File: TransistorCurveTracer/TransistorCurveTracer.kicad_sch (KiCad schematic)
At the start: 24 parts, among them J1 Conn_01x04_Pin, J2 Conn_01x04_Pin, J3 Conn_01x04_Pin, Q1 BC547, U1 NE555P, U3 MCP601-xP

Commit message: in progress
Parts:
- added Q2: BC547, Package_TO_SOT_THT:TO-92_Inline, symbol Transistor_BJT:BC547
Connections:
- net GND: now also Q2.3 (E)
- net Pulse1: now also Q2.2 (B)
- net NC renamed ResetStairStep
- net ResetStairStep: now also Q2.1 (C)
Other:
- note added: "Module 1 NE555"
- note added: "Module2 Reset NE555 + reset StairStep"
- moved on the sheet: C1, C2, C3, C4, D1, D2, D3, D4, J1, J2, J3, Q1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

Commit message: in progress
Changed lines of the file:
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@@
       (effects (font (size 1.27 1.27)) (justify left))
     )
-    (property "Value" "6.8k" (at 149.86 92.71 0)
+    (property "Value" "6.8k" (at 149.86 93.98 0)
       (effects (font (size 1.27 1.27)) (justify left))
     )

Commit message: curve tracer in progress
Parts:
- added C5: 100n, Capacitor_SMD:C_0805_2012Metric_Pad1.18x1.45mm_HandSolder, symbol Device:C
- added C6: 10n, Capacitor_SMD:C_1206_3216Metric_Pad1.33x1.80mm_HandSolder, symbol Device:C
- added Q3: BC547, Package_TO_SOT_THT:TO-92_Inline, symbol Transistor_BJT:BC547
- added Q4, Q5: 2N2907, symbol Simulation_SPICE:PNP
- added Q6: DUT, Package_TO_SOT_THT:TO-92_Inline, symbol Transistor_BJT:BC547
- added R11, R12, R13, R14, R15, R18: 10k, Resistor_SMD:R_1206_3216Metric_Pad1.30x1.75mm_HandSolder, symbol Device:R
- added R16, R17: 3.9k, Resistor_SMD:R_1206_3216Metric_Pad1.30x1.75mm_HandSolder, symbol Device:R
- added R19: 470k, Resistor_SMD:R_1206_3216Metric_Pad1.30x1.75mm_HandSolder, symbol Device:R
- added R20: 270k, Resistor_SMD:R_1206_3216Metric_Pad1.30x1.75mm_HandSolder, symbol Device:R
- added U2, U4: MCP601-xP, Package_DIP:DIP-8_W7.62mm, symbol Amplifier_Operational:MCP601-xP
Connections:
- net GND: now also U3.7 (V+), C5.2, C6.2, Q3.3 (E), Q6.3 (E), R12.2, R17.2, R20.2, U2.7 (V+), U4.7 (V+); no longer U3.4 (V-)
- net Out555: now also R11.2, R16.2
- net ResetStairStep: now also C5.1, R11.1, R14.2, U2.3 (+)
- net Vcc: now also U3.4 (V-), R15.1, U2.4 (V-), U4.4 (V-); no longer U3.7 (V+)
- net at R1.1, R2.1, R3.1: now also U3.3 (+); no longer U3.2 (-)
- net at C1.1, D1.1 (K), D2.2 (A): now also U3.2 (-); no longer U3.3 (+)
- new net: R12.1, R13.2, U2.2 (-)
- new net: R17.1, R18.2, U4.2 (-)
- new net: C6.1, Q3.1 (C), R15.2, U4.3 (+)
- new net: Q6.2 (B), R19.2
- new net: Q3.2 (B), R16.1
- new net SawTooth: Q4.3 (E), Q5.3 (E), R18.1, U4.6
- new net StairStep: R13.1, R14.1, R19.1, U2.6
- new net X: Q4.1 (C), Q4.2 (B), Q5.2 (B), Q6.1 (C)
- new net Y: Q5.1 (C), R20.1
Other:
- note added: "In1 : StairStep In2 : GNG In3 : SawTooth Out1 : X Out2 : Y"
- note added: "In1 : Vcc In2 : GND In3 : Out555 In4 : ResetStairStep Out : StairStep"
- note added: "In1 : Vcc In2 : GND In3 : Out555 Out : SawTooth"
- note added: "In1 : Vcc In2 : GND In3 : Reset555 Out : Out555"
- note added: "In1 : Vcc In2 : GND Out1: ResetStairStep Out2: Reset555"
- note added: "Module 3 StairStep"
- note added: "Module 4 SawTooth"
- note added: "Module 5 Out X Y"

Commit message: TransistorCurveTracer in progress
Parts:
- added J4: Conn_01x04_Pin, Connector_PinHeader_2.54mm:PinHeader_1x04_P2.54mm_Vertical, symbol Connector:Conn_01x04_Pin
- added J5, J6: Conn_01x05_Pin, Connector_PinHeader_2.54mm:PinHeader_1x05_P2.54mm_Vertical, symbol Connector:Conn_01x05_Pin
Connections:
- net GND: now also J4.2 (Pin_2), J5.2 (Pin_2), J6.2 (Pin_2)
- net Out555: now also J4.3 (Pin_3), J5.3 (Pin_3)
- net ResetStairStep: now also J5.4 (Pin_4)
- net SawTooth: now also J4.4 (Pin_4), J6.3 (Pin_3)
- net StairStep: now also J5.5 (Pin_5), J6.1 (Pin_1)
- net Vcc: now also J4.1 (Pin_1), J5.1 (Pin_1)
- net X: now also J6.4 (Pin_4)
- net Y: now also J6.5 (Pin_5)
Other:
- moved on the sheet: C5, C6, Q3, Q4, Q5, Q6, R11, R12, R13, R14, R15, R16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

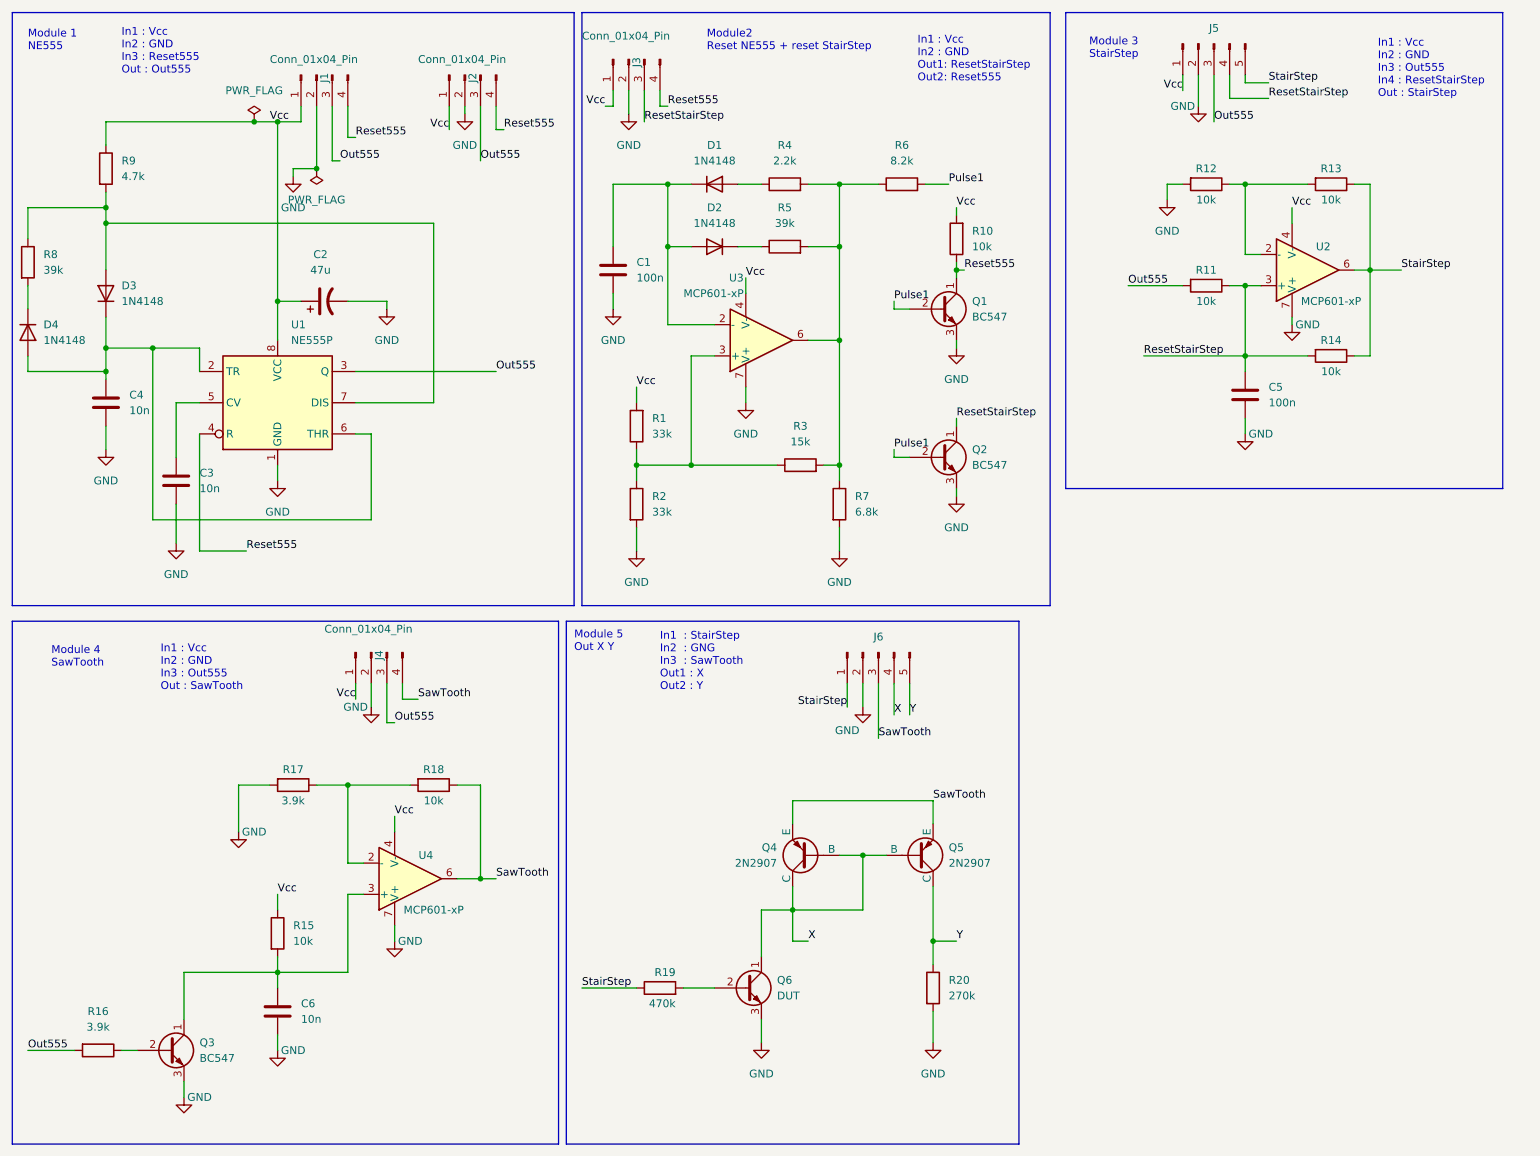
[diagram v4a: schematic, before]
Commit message: fix VCC/GND VDD/VSS in progress
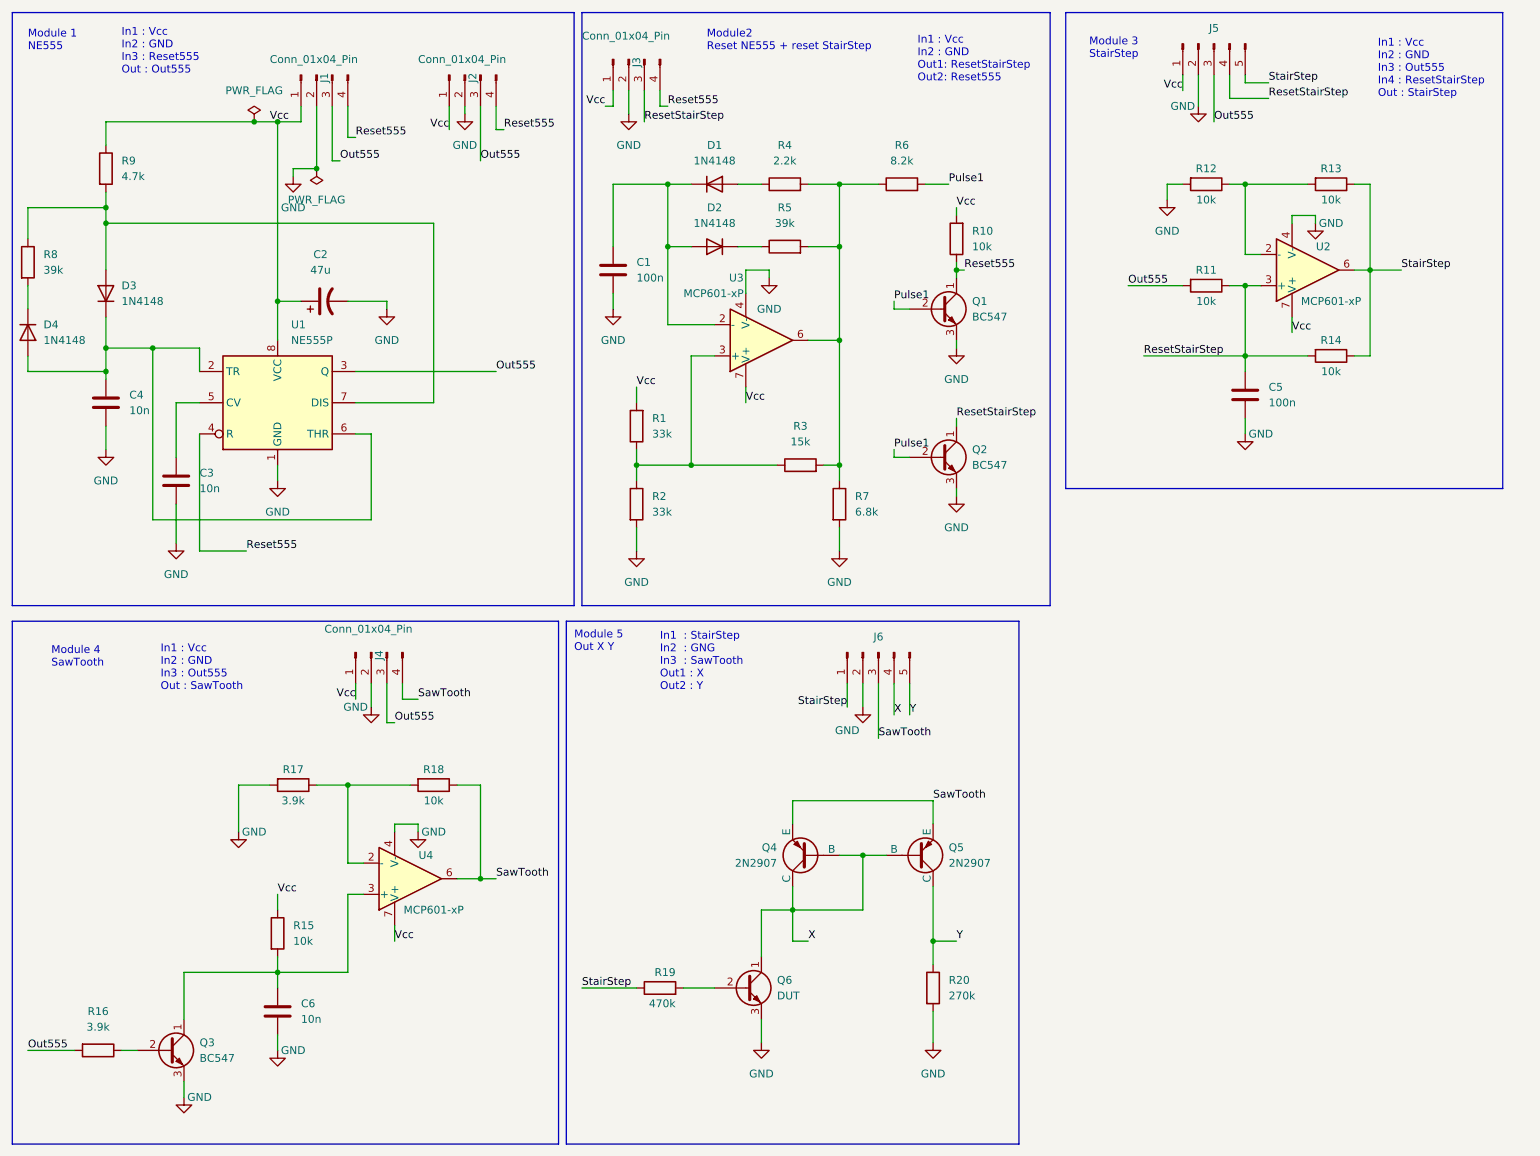
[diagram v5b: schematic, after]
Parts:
- Q4, Q5: footprint (none) -> Package_TO_SOT_THT:TO-92_Inline
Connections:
- net GND: now also U2.4 (V-), U3.4 (V-), U4.4 (V-); no longer U2.7 (V+), U3.7 (V+), U4.7 (V+)
- net Vcc: now also U2.7 (V+), U3.7 (V+), U4.7 (V+); no longer U2.4 (V-), U3.4 (V-), U4.4 (V-)

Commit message: 5 modules
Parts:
- removed J1, J2, J3, J4: Conn_01x04_Pin, Connector_PinHeader_2.54mm:PinHeader_1x04_P2.54mm_Vertical, symbol Connector:Conn_01x04_Pin
- removed J5, J6: Conn_01x05_Pin, Connector_PinHeader_2.54mm:PinHeader_1x05_P2.54mm_Vertical, symbol Connector:Conn_01x05_Pin
- added J1, J2, J3, J4, J5: Conn_01x06_Pin, Connector_PinHeader_2.54mm:PinHeader_1x06_P2.54mm_Horizontal, symbol Connector:Conn_01x06_Pin
- added RV1: 0-5k, Connector_PinSocket_2.54mm:PinSocket_1x03_P2.54mm_Vertical, symbol Device:R_Potentiometer_US
- C1: renamed from C4; footprint Capacitor_SMD:C_0805_2012Metric_Pad1.18x1.45mm_HandSolder -> Capacitor_THT:C_Disc_D7.5mm_W2.5mm_P5.00mm
- C2: renamed from C3; footprint Capacitor_SMD:C_1206_3216Metric_Pad1.33x1.80mm_HandSolder -> Capacitor_THT:C_Disc_D7.5mm_W2.5mm_P5.00mm
- C3: renamed from C6; footprint Capacitor_SMD:C_1206_3216Metric_Pad1.33x1.80mm_HandSolder -> Capacitor_THT:C_Disc_D7.5mm_W2.5mm_P5.00mm
- C5: renamed from C1; footprint Capacitor_SMD:C_0805_2012Metric_Pad1.18x1.45mm_HandSolder -> Capacitor_THT:C_Disc_D7.5mm_W2.5mm_P5.00mm
- C6: renamed from C5; footprint Capacitor_SMD:C_0805_2012Metric_Pad1.18x1.45mm_HandSolder -> Capacitor_THT:C_Disc_D7.5mm_W2.5mm_P5.00mm
- D1: renamed from D4; footprint Diode_SMD:D_1812_4532Metric_Pad1.30x3.40mm_HandSolder -> Diode_THT:D_DO-15_P15.24mm_Horizontal
- D2: renamed from D3; footprint Diode_SMD:D_1812_4532Metric_Pad1.30x3.40mm_HandSolder -> Diode_THT:D_DO-15_P15.24mm_Horizontal
- D3: renamed from D1; footprint Diode_SMD:D_1812_4532Metric_Pad1.30x3.40mm_HandSolder -> Diode_THT:D_DO-15_P15.24mm_Horizontal
- D4: renamed from D2; footprint Diode_SMD:D_1812_4532Metric_Pad1.30x3.40mm_HandSolder -> Diode_THT:D_DO-15_P15.24mm_Horizontal
- R1: renamed from R8; footprint Resistor_THT:R_Axial_DIN0207_L6.3mm_D2.5mm_P2.54mm_Vertical -> Resistor_THT:R_Axial_DIN0411_L9.9mm_D3.6mm_P15.24mm_Horizontal
- R10: renamed from R19; footprint Resistor_SMD:R_1206_3216Metric_Pad1.30x1.75mm_HandSolder -> Resistor_THT:R_Axial_DIN0411_L9.9mm_D3.6mm_P15.24mm_Horizontal
- R11: renamed from R4; value 2.2k -> 1k; footprint Resistor_SMD:R_1206_3216Metric_Pad1.30x1.75mm_HandSolder -> Resistor_THT:R_Axial_DIN0411_L9.9mm_D3.6mm_P15.24mm_Horizontal
- R12: renamed from R5; footprint Resistor_THT:R_Axial_DIN0207_L6.3mm_D2.5mm_P2.54mm_Vertical -> Resistor_THT:R_Axial_DIN0411_L9.9mm_D3.6mm_P15.24mm_Horizontal
- R13: renamed from R3; footprint Resistor_THT:R_Axial_DIN0207_L6.3mm_D2.5mm_P2.54mm_Vertical -> Resistor_THT:R_Axial_DIN0411_L9.9mm_D3.6mm_P15.24mm_Horizontal
- R14: renamed from R7; footprint Resistor_SMD:R_1206_3216Metric_Pad1.30x1.75mm_HandSolder -> Resistor_THT:R_Axial_DIN0411_L9.9mm_D3.6mm_P15.24mm_Horizontal
- R15: renamed from R6; footprint Resistor_SMD:R_1206_3216Metric_Pad1.30x1.75mm_HandSolder -> Resistor_THT:R_Axial_DIN0411_L9.9mm_D3.6mm_P15.24mm_Horizontal
- R16: renamed from R20; footprint Resistor_SMD:R_1206_3216Metric_Pad1.30x1.75mm_HandSolder -> Resistor_THT:R_Axial_DIN0411_L9.9mm_D3.6mm_P15.24mm_Horizontal
- R17: renamed from R12; footprint Resistor_SMD:R_1206_3216Metric_Pad1.30x1.75mm_HandSolder -> Resistor_THT:R_Axial_DIN0411_L9.9mm_D3.6mm_P15.24mm_Horizontal
- R18: renamed from R11; footprint Resistor_SMD:R_1206_3216Metric_Pad1.30x1.75mm_HandSolder -> Resistor_THT:R_Axial_DIN0411_L9.9mm_D3.6mm_P15.24mm_Horizontal
- R19: renamed from R13; footprint Resistor_SMD:R_1206_3216Metric_Pad1.30x1.75mm_HandSolder -> Resistor_THT:R_Axial_DIN0411_L9.9mm_D3.6mm_P15.24mm_Horizontal
- R2: renamed from R16; footprint Resistor_SMD:R_1206_3216Metric_Pad1.30x1.75mm_HandSolder -> Resistor_THT:R_Axial_DIN0411_L9.9mm_D3.6mm_P15.24mm_Horizontal
- R20: renamed from R14; footprint Resistor_SMD:R_1206_3216Metric_Pad1.30x1.75mm_HandSolder -> Resistor_THT:R_Axial_DIN0411_L9.9mm_D3.6mm_P15.24mm_Horizontal
- R3: renamed from R9; footprint Resistor_SMD:R_1206_3216Metric_Pad1.30x1.75mm_HandSolder -> Resistor_THT:R_Axial_DIN0411_L9.9mm_D3.6mm_P15.24mm_Horizontal
- R4: renamed from R15; footprint Resistor_SMD:R_1206_3216Metric_Pad1.30x1.75mm_HandSolder -> Resistor_THT:R_Axial_DIN0411_L9.9mm_D3.6mm_P15.24mm_Horizontal
- R5: renamed from R17; footprint Resistor_SMD:R_1206_3216Metric_Pad1.30x1.75mm_HandSolder -> Resistor_THT:R_Axial_DIN0411_L9.9mm_D3.6mm_P15.24mm_Horizontal
- R6: renamed from R18; footprint Resistor_SMD:R_1206_3216Metric_Pad1.30x1.75mm_HandSolder -> Resistor_THT:R_Axial_DIN0411_L9.9mm_D3.6mm_P15.24mm_Horizontal
- R7: renamed from R10; footprint Resistor_SMD:R_1206_3216Metric_Pad1.30x1.75mm_HandSolder -> Resistor_THT:R_Axial_DIN0411_L9.9mm_D3.6mm_P15.24mm_Horizontal
- R8: renamed from R1; footprint Resistor_SMD:R_1206_3216Metric_Pad1.30x1.75mm_HandSolder -> Resistor_THT:R_Axial_DIN0411_L9.9mm_D3.6mm_P15.24mm_Horizontal
- R9: renamed from R2; footprint Resistor_SMD:R_1206_3216Metric_Pad1.30x1.75mm_HandSolder -> Resistor_THT:R_Axial_DIN0411_L9.9mm_D3.6mm_P15.24mm_Horizontal
- renumbered C2 to C4, Q3 to Q1, Q1 to Q2, Q6 to Q3, Q2 to Q6, U4 to U2, U2 to U4
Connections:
- net GND: now also J1.6 (Pin_6), J2.6 (Pin_6), J3.6 (Pin_6), J4.6 (Pin_6), J5.6 (Pin_6)
- net Out555: now also J1.3 (Pin_3), J2.3 (Pin_3), J3.3 (Pin_3), J4.3 (Pin_3), J5.3 (Pin_3)
- net SawTooth: now also J1.5 (Pin_5), J2.5 (Pin_5), J3.5 (Pin_5), J4.5 (Pin_5), J5.5 (Pin_5)
- net StairStep: now also J1.4 (Pin_4), J2.4 (Pin_4), J3.4 (Pin_4), J4.4 (Pin_4), J5.4 (Pin_4)
- net Vcc: now also J1.1 (Pin_1), J2.1 (Pin_1), J3.1 (Pin_1), J4.1 (Pin_1), J5.1 (Pin_1)
- net at R12.2, R13.2, R14.1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: now also RV1.2, RV1.3; no longer R11.2
- net Pulse1 renamed SignalReset
- net SignalReset: now also J1.2 (Pin_2), J2.2 (Pin_2), J3.2 (Pin_2), J4.2 (Pin_2), J5.2 (Pin_2)
- net ResetStairStep: no longer names the net of C6.1, Q6.1 (C), R18.1, R20.2, U4.3 (+)
- new net: R11.2, RV1.1
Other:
- note added: "In1 : GND In2 : StairStep In3 : SawTooth Out1 : X Out2 : Y"
- note added: "In1 : Vcc In2 : GND In3 : Out555 In4 : SignalReset Out : StairStep"
- note added: "In1 : Vcc In2 : GND In3 : SignalReset Out : Out555"
- note added: "In1 : Vcc In2 : GND In4 : Out555 Out : SawTooth"
- note added: "In1 : Vcc In2 : GND Out1: SignalReset"
- note added: "Module 5"
- note added: "Module2 SignalReset"
- note removed: "In1 : StairStep In2 : GNG In3 : SawTooth Out1 : X Out2 : Y"
- note removed: "In1 : Vcc In2 : GND In3 : Out555 In4 : ResetStairStep Out : StairStep"
- note removed: "In1 : Vcc In2 : GND In3 : Out555 Out : SawTooth"
- note removed: "In1 : Vcc In2 : GND In3 : Reset555 Out : Out555"
- note removed: "In1 : Vcc In2 : GND Out1: ResetStairStep Out2: Reset555"
- note removed: "Module 5 Out X Y"
- note removed: "Module2 Reset NE555 + reset StairStep"
- moved on the sheet: C6, Q2, Q6, R11, R14, R15, R17, R18, R19, R20, R7, U4
